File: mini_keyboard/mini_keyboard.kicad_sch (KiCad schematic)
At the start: 4 parts, among them U1 MX1A-11NN, U2 MX1A-11NN, U3 MX1A-11NN, U4 MX1A-11NN

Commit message: adding more keys and looking at spacing
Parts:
- added U10, U11, U12, U5, U6, U7, U8, U9: MX1A-11NN, pedrolib:CHERRY_MX1A-11NN_SWITCH, symbol pedrolib:MX1A-11NN
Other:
- moved on the sheet: U3, U4

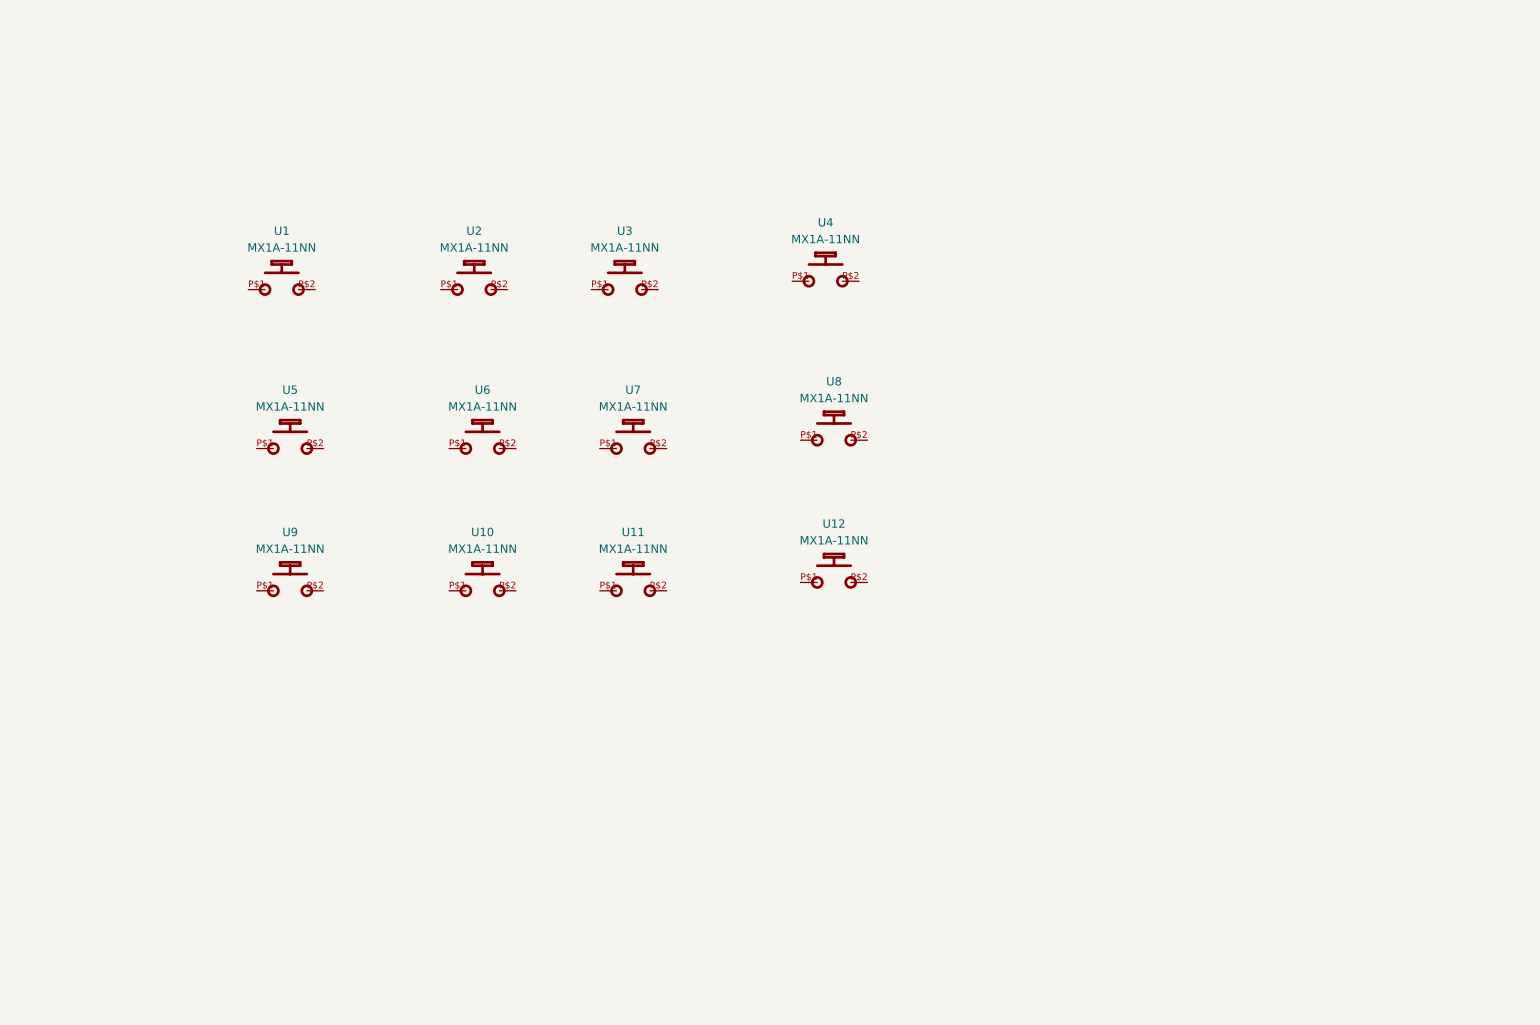
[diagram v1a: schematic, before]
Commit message: updating library for keyboard work
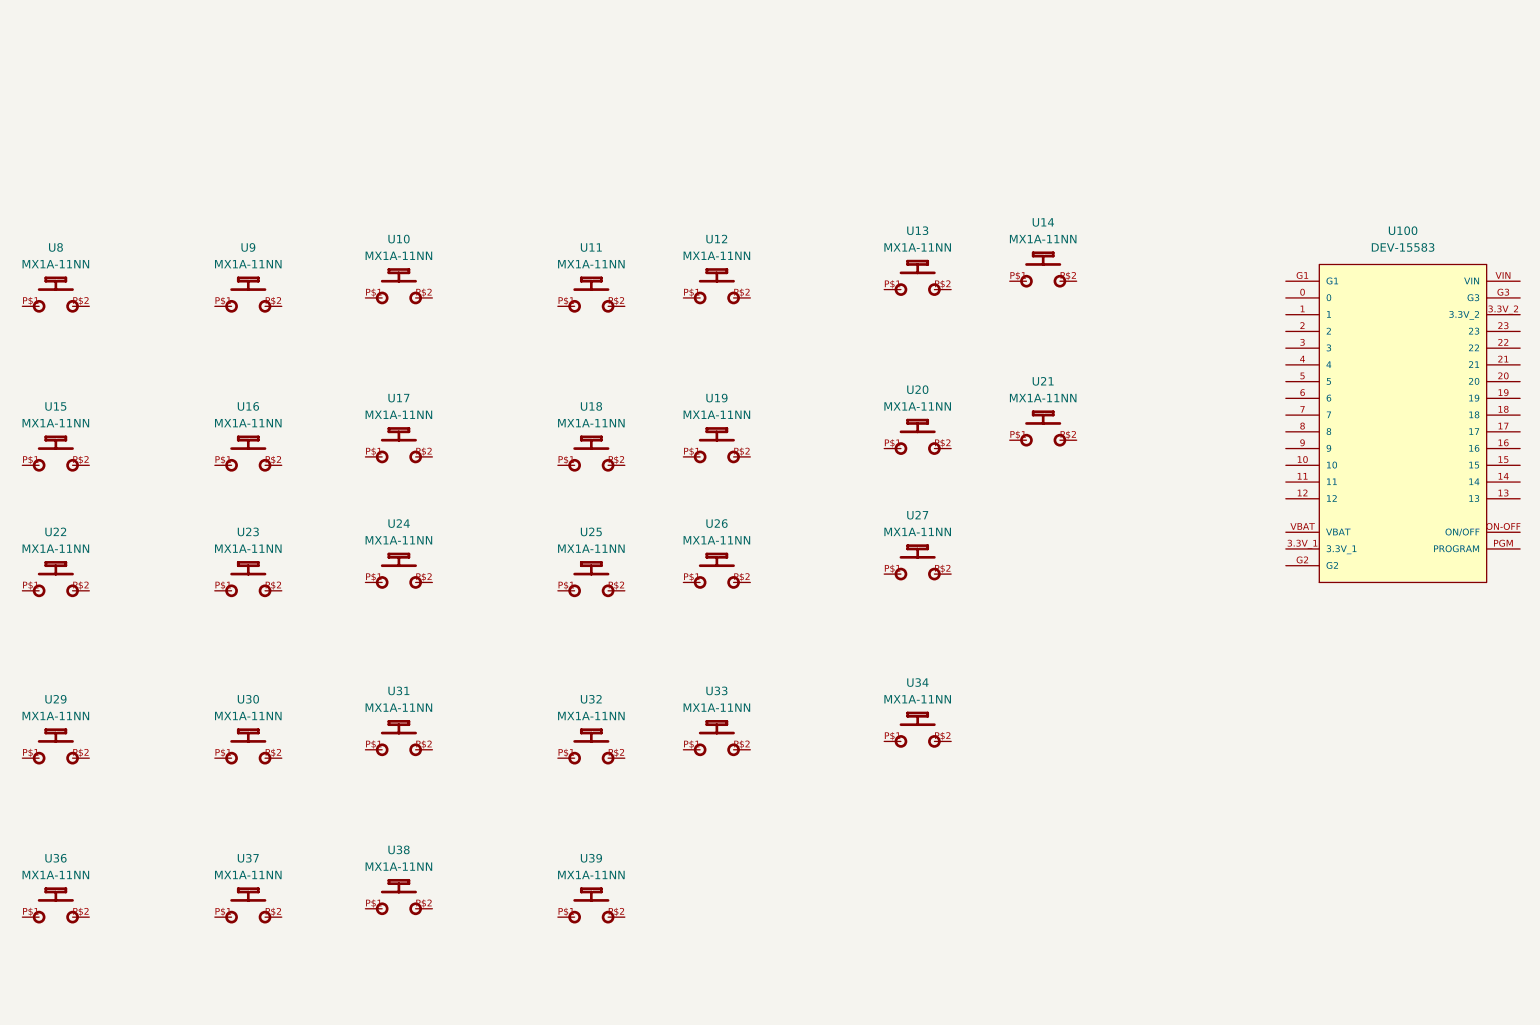
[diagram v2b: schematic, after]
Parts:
- removed U1, U2, U3, U4, U5, U6, U7: MX1A-11NN, pedrolib:CHERRY_MX1A-11NN_SWITCH, symbol pedrolib:MX1A-11NN
- added U100: DEV-15583, pedrolib:MODULE_DEV-15583, symbol pedrolib:DEV-15583
- added U13, U14, U15, U16, U17, U18, U19, U20, U21, U22, U23, U24, U25, U26, U27, U29, U30, U31, U32, U33, U34, U36, U37, U38, U39: MX1A-11NN, pedrolib:CHERRY_MX1A-11NN_SWITCH, symbol pedrolib:MX1A-11NN
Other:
- moved on the sheet: U10, U11, U12, U8, U9

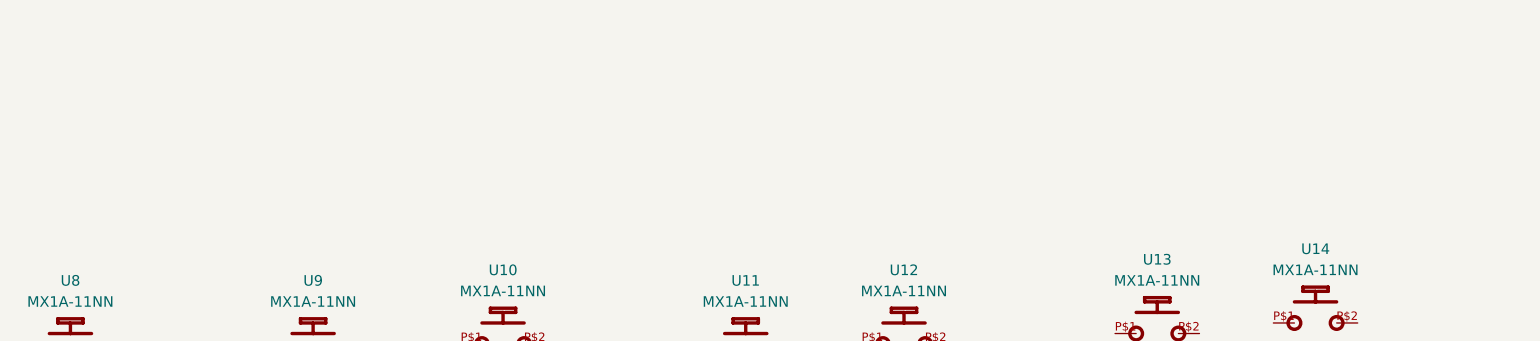
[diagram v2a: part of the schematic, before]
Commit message: added Teensy 4.0
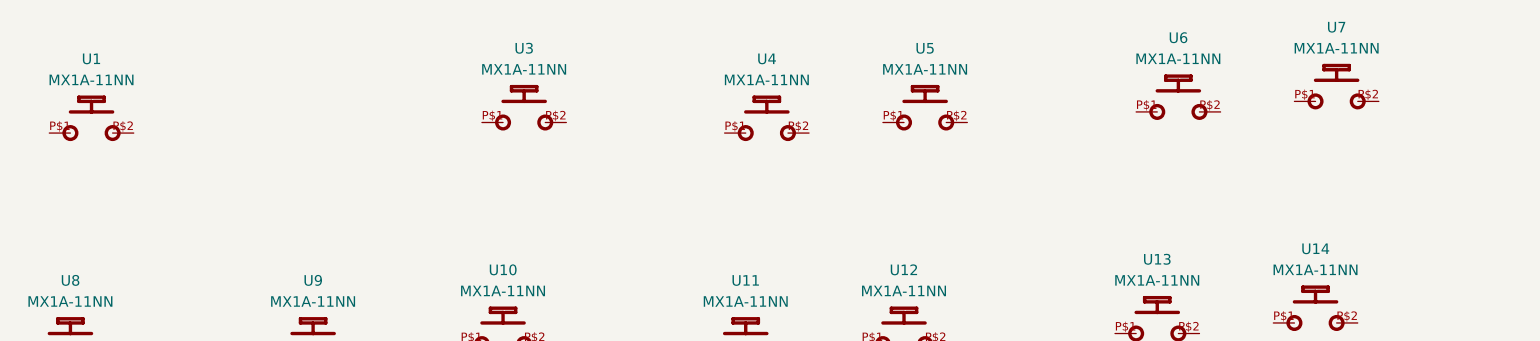
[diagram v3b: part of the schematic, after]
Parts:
- added U1, U3, U4, U5, U6, U7: MX1A-11NN, pedrolib:CHERRY_MX1A-11NN_SWITCH, symbol pedrolib:MX1A-11NN

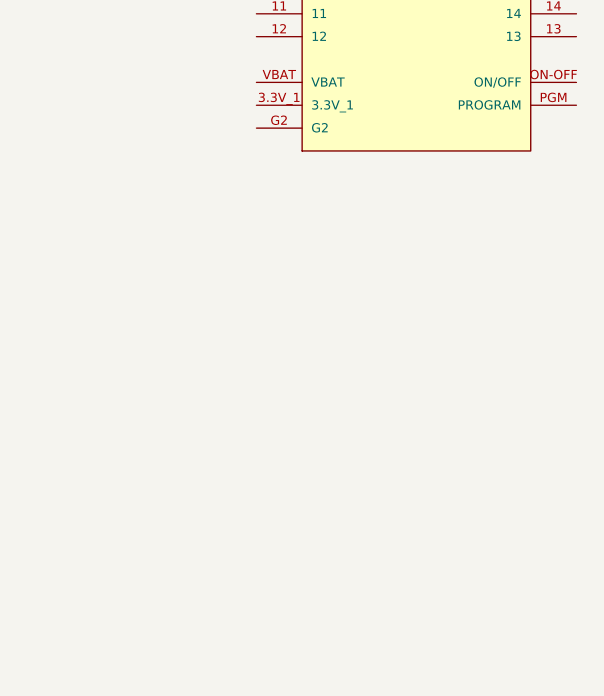
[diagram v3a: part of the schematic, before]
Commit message: Looking at Arduino 33 IOT for CPU to get arduino-cli support
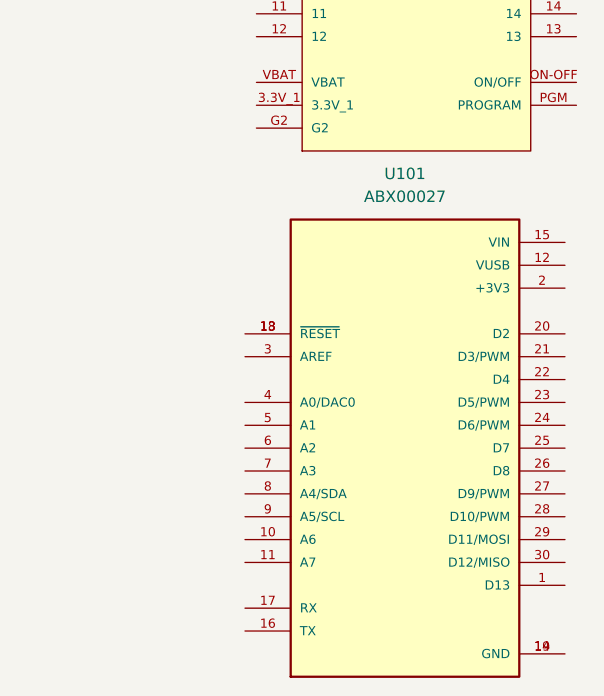
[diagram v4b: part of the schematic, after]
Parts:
- added U101: ABX00027, pedrolib:MODULE_ABX00027, symbol pedrolib:ABX00027
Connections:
- new net: U101.13 (~{RESET}), U101.18 (~{RESET})
- new net: U101.14 (GND), U101.19 (GND)

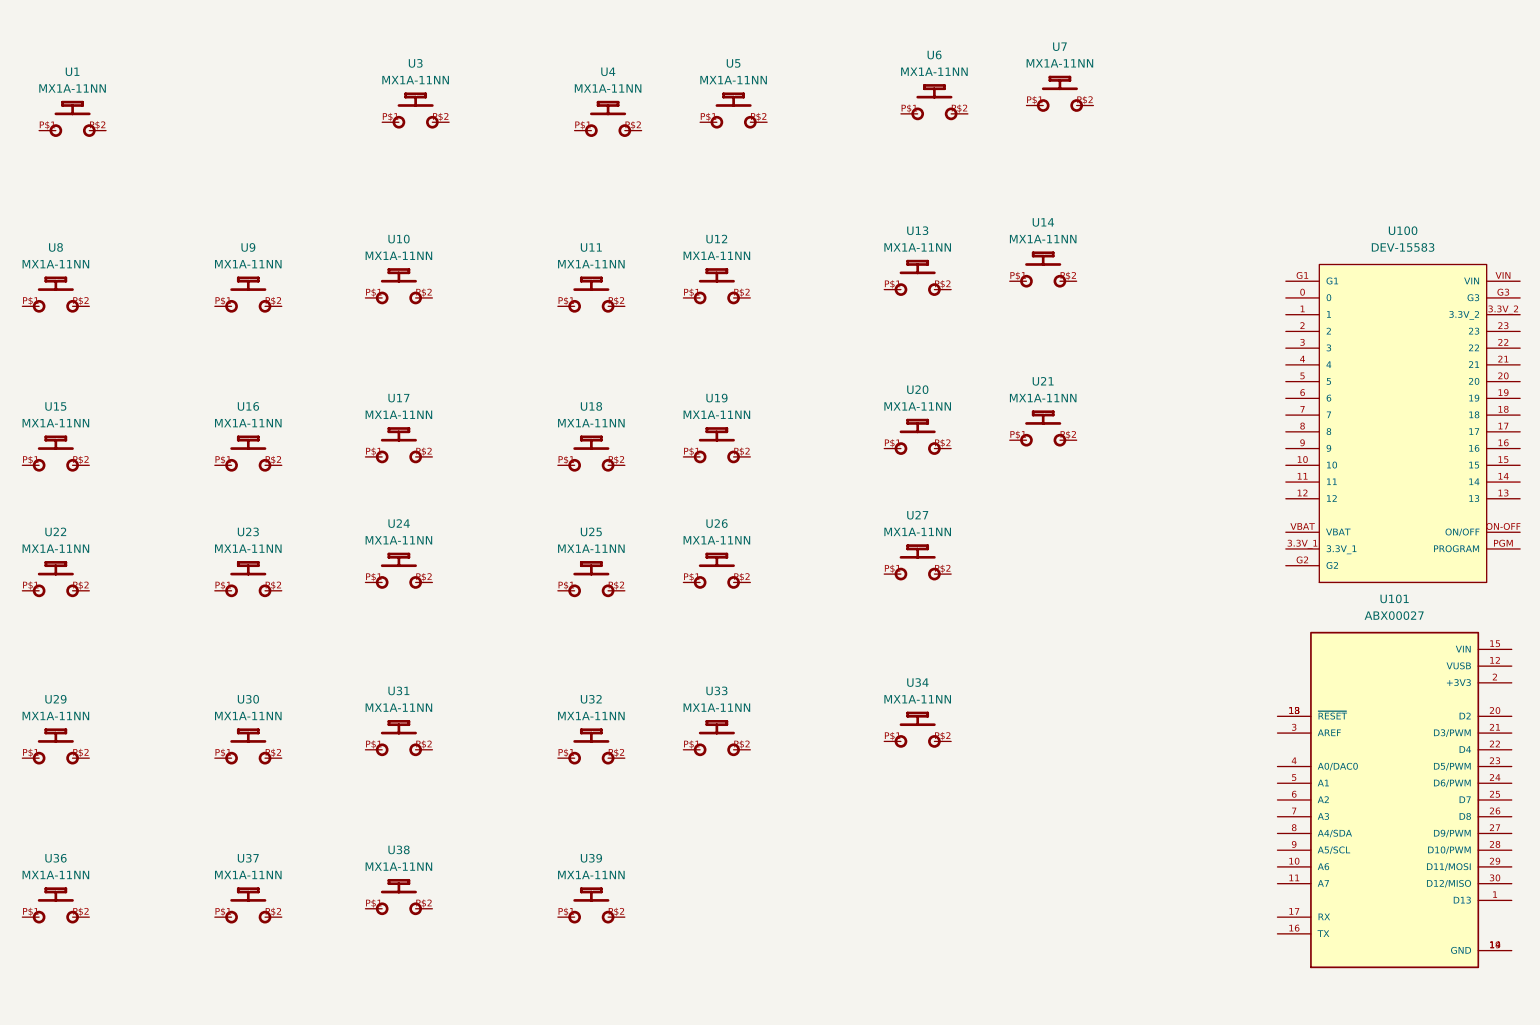
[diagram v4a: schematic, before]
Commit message: prepping to wire the switches and diodes to the array
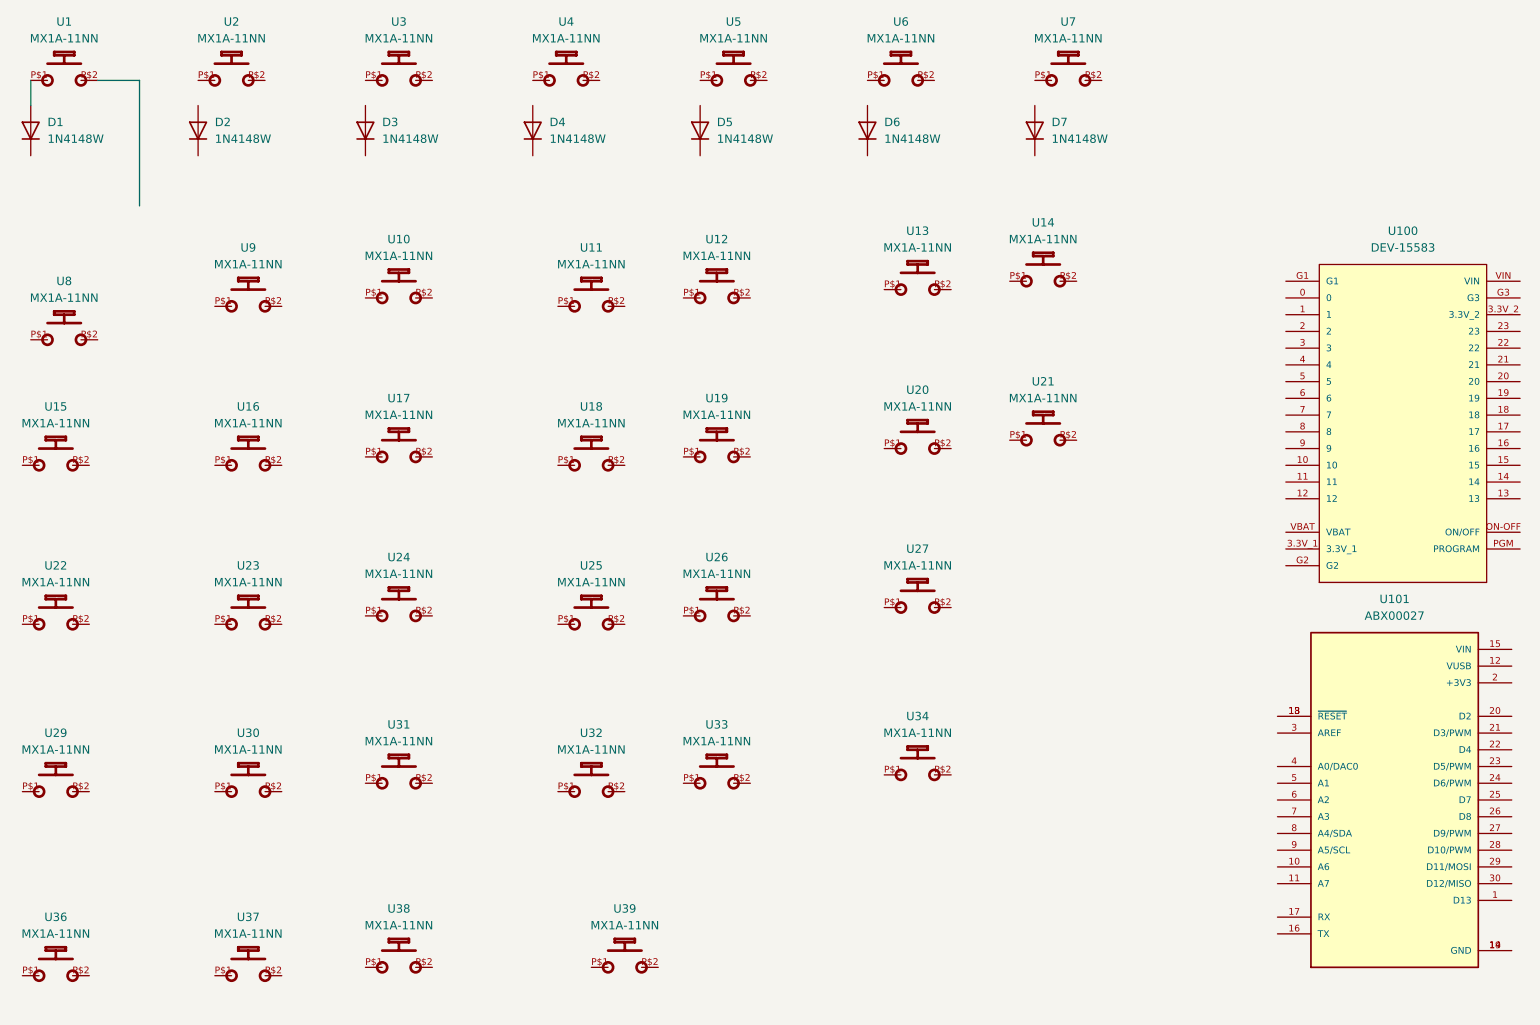
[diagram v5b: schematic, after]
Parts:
- added D1, D2, D3, D4, D5, D6, D7: 1N4148W, Diode_SMD:D_SOD-123, symbol Diode:1N4148W
- added U2: MX1A-11NN, pedrolib:CHERRY_MX1A-11NN_SWITCH, symbol pedrolib:MX1A-11NN
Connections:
- net at U1.P$1: now also D1.2 (A)
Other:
- moved on the sheet: U1, U22, U23, U24, U25, U26, U27, U29, U3, U30, U31, U32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
